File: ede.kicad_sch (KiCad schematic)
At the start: 111 parts, among them J1 Conn_01x01, J10 Conn_01x01, J11 Conn_01x01, J12 Conn_01x01, J2 Conn_01x01, J3 Conn_01x01, J4 Conn_01x01, J5 Conn_01x06, J6 Conn_01x01, J7 Conn_01x04, J8 Conn_01x04, J9 Conn_01x01, Q1 MDP10N027, Q2 MDP10N027, Q3 MDP10N027, Q4 MDP10N027, Q5 MDP10N027, Q6 MDP10N027, U1 YAAJ_BluePill, U2 NCS20034DR2G, U3 STH0548S12, U4 MP1584EN_4pin, U5 U3216, U6 U3216, U7 U3216

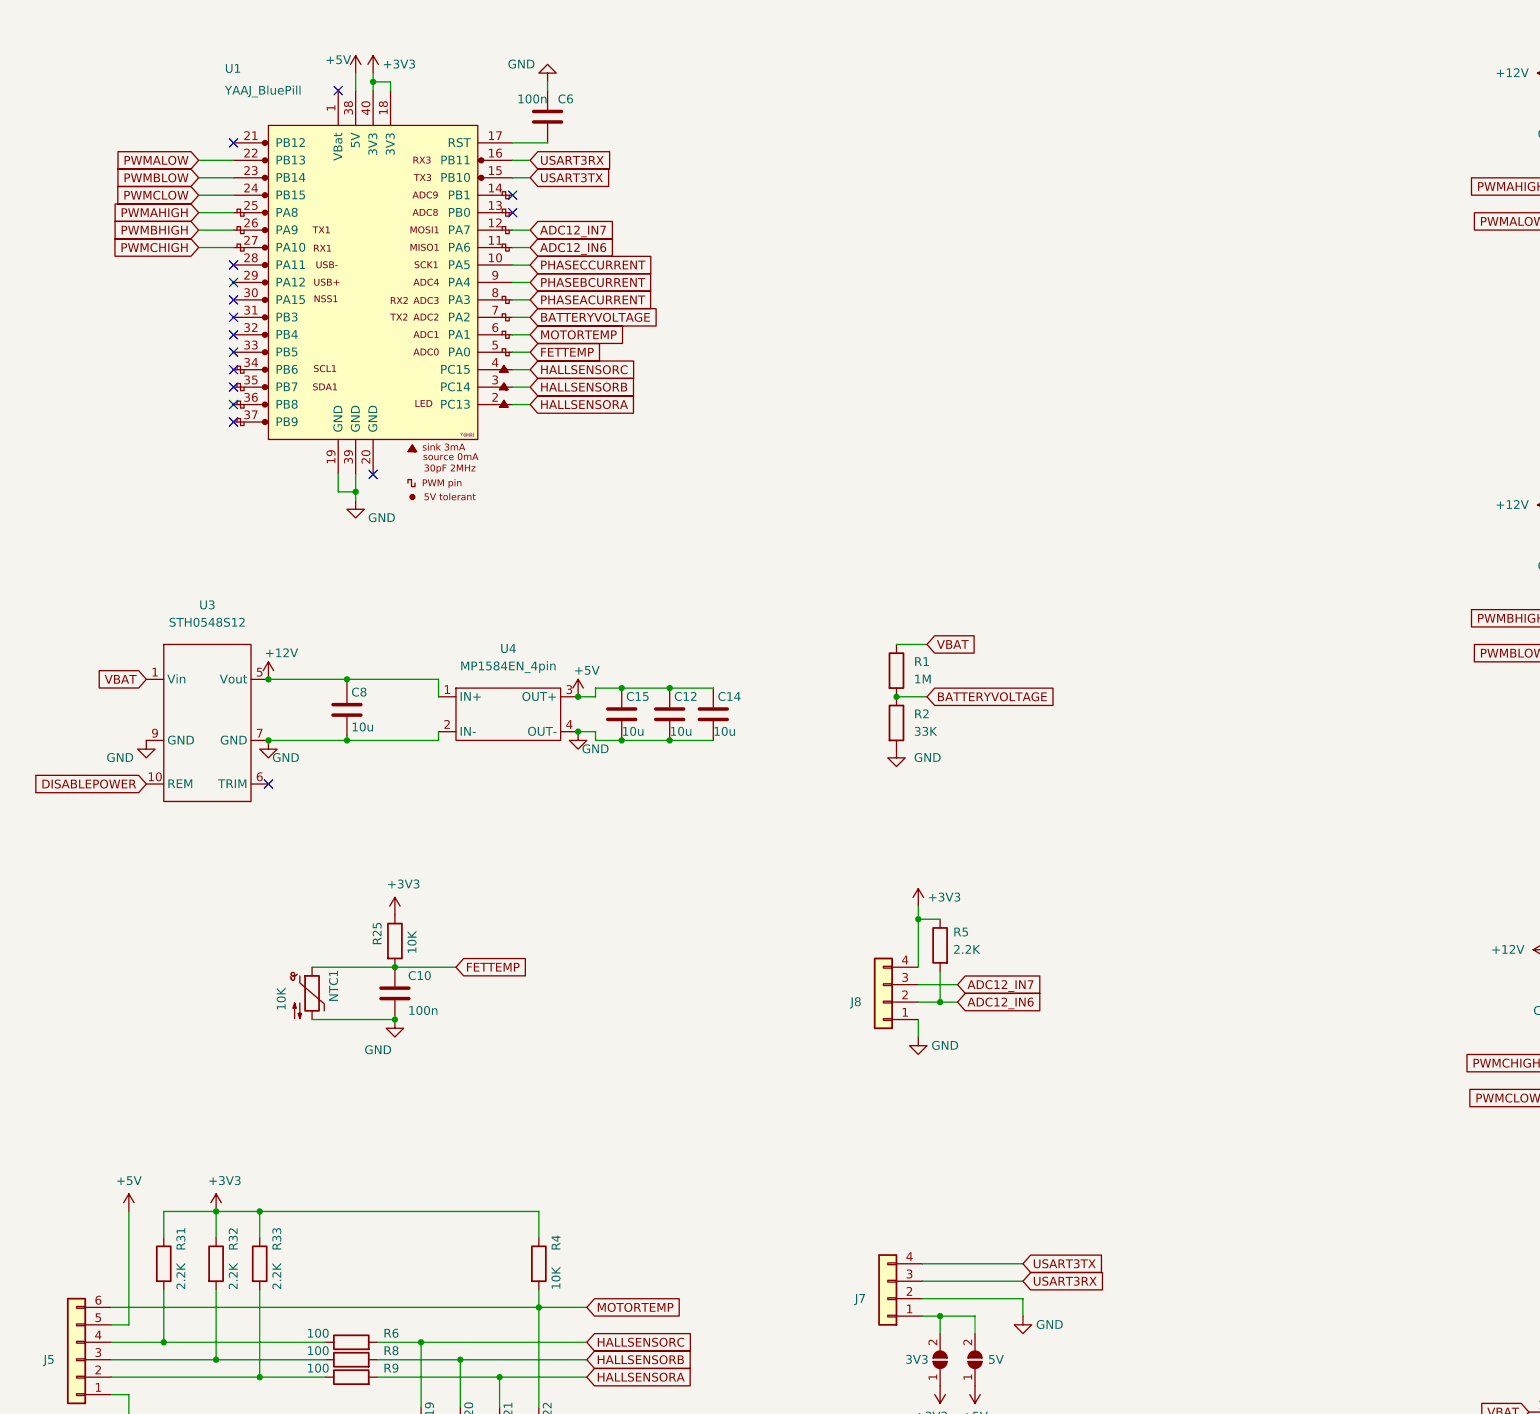
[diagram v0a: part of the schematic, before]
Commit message: sch: blackpill instead of bluepill
Firmware for this project only supports blackpill ATM. Reflect it in
schematic, note pcb layout used is same as in v0.5.x .

Signed-off-by: Afzal <afzal@intible.in>
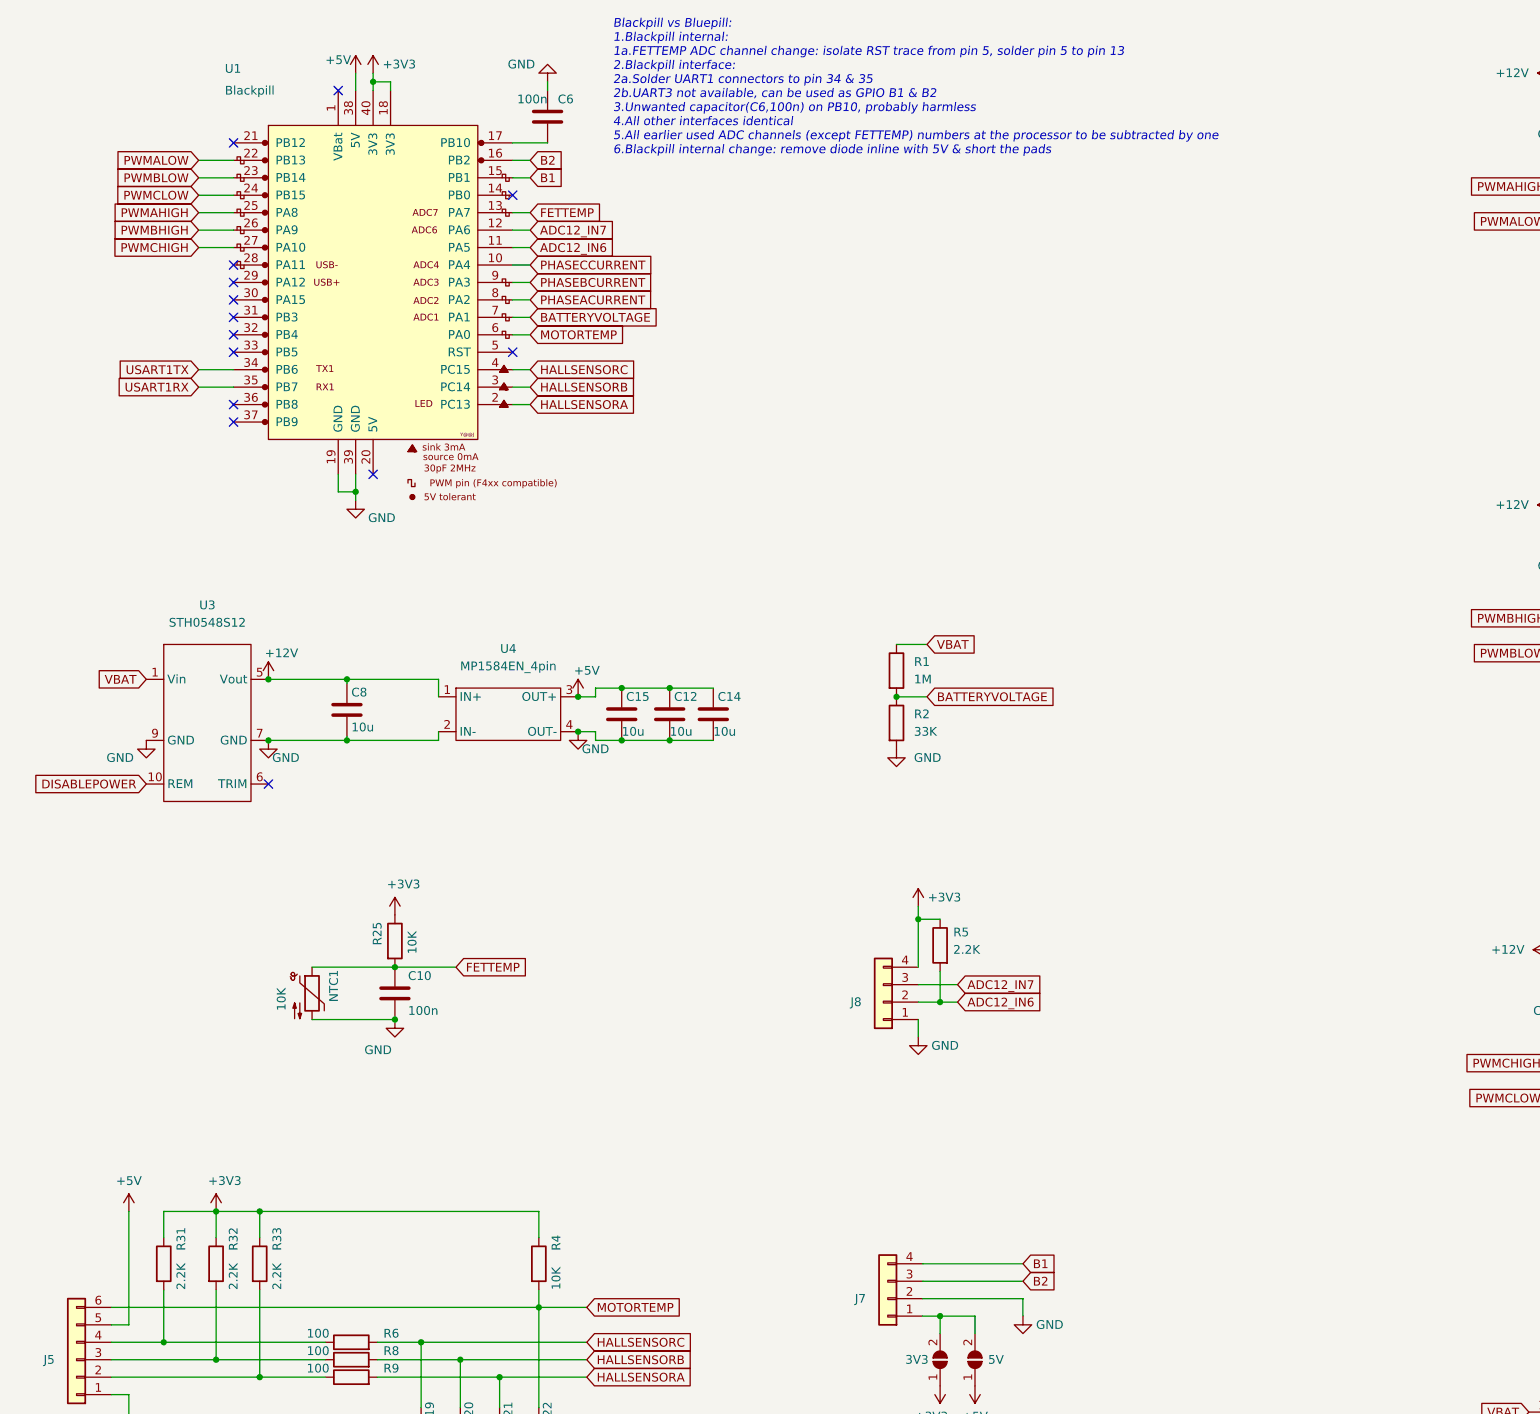
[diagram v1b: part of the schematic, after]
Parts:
- U1: value YAAJ_BluePill -> Blackpill; footprint Intible:YAAJ_Bluepill -> (none); symbol Bluepill_Module:YAAJ_BluePill -> Bluepill_Module:Blackpill; now in the parts list
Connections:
- net FETTEMP: now also U1.13 (PA7); no longer U1.5 (PA0)
- net USART1TX: now reaches U1.34 (PB6)
- net USART1RX: now reaches U1.35 (PB7)
- net USART3RX renamed B2
- net USART3TX renamed B1
- no-connect marks 16 -> 14
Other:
- note added: "Blackpill vs Bluepill: 1.Blackpill internal: 1a.FETTEMP ADC channel change: isolate RST trace from pin 5, solder pin 5 to pin 13 2.Blackpill interface: 2a.Solder UART1 connectors to pin 34 & 35 2b.UART3 not available, can be used as GPIO B1 & B2 3.Unwanted capacitor(C6,100n) on PB10, probably harmless 4.All other interfaces identical 5.All earlier used ADC channels (except FETTEMP) numbers at the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"
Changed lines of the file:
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@@
   (no_connect (at 46.99 50.8))
   (no_connect (at 46.99 48.26))
-  (no_connect (at 87.63 40.64))
   (no_connect (at 62.23 22.86))
   (no_connect (at 87.63 38.1))
@@
   (no_connect (at 46.99 53.34))
   (no_connect (at 46.99 58.42))
-  (no_connect (at 46.99 63.5))
   (no_connect (at 46.99 68.58))
   (no_connect (at 46.99 60.96))
-  (no_connect (at 46.99 66.04))
   (no_connect (at 46.99 30.48))
   (no_connect (at 46.99 71.12))
+  (no_connect (at 87.63 60.96))
   (wire (pts (xy 50.8 186.055) (xy 50.8 189.865))
     (stroke (width 0) (type default) (color 0 0 0 0))
@@
     (stroke (width 0) (type default) (color 0 0 0 0))
   )
+  (wire (pts (xy 41.91 63.5) (xy 46.99 63.5))
+    (stroke (width 0) (type default) (color 0 0 0 0))
+  )
   (wire (pts (xy 110.49 117.475) (xy 103.505 117.475))
     (stroke (width 0) (type default) (color 0 0 0 0))
@@
     (stroke (width 0) (type default) (color 0 0 0 0))
   )
+  (wire (pts (xy 41.91 66.04) (xy 46.99 66.04))
+    (stroke (width 0) (type default) (color 0 0 0 0))
+  )
   (wire (pts (xy 313.055 38.1) (xy 313.055 40.64))
     (stroke (width 0) (type default) (color 0 0 0 0))
@@
     (stroke (width 0) (type default) (color 0 0 0 0))
   )
+  (wire (pts (xy 87.63 35.56) (xy 90.17 35.56))
+    (stroke (width 0) (type default) (color 0 0 0 0))
+  )
   (wire (pts (xy 286.385 90.805) (xy 290.195 90.805))
     (stroke (width 0) (type default) (color 0 0 0 0))
@@
     (stroke (width 0) (type default) (color 0 0 0 0))
   )
-  (wire (pts (xy 87.63 35.56) (xy 90.17 35.56))
-    (stroke (width 0) (type default) (color 0 0 0 0))
-  )
   (wire (pts (xy 41.91 35.56) (xy 46.99 35.56))
     (stroke (width 0) (type default) (color 0 0 0 0))
@@
     (stroke (width 0) (type default) (color 0 0 0 0))
   )
+  (wire (pts (xy 87.63 40.64) (xy 90.17 40.64))
+    (stroke (width 0) (type default) (color 0 0 0 0))
+  )
   (wire (pts (xy 302.895 118.745) (xy 313.055 118.745))
     (stroke (width 0) (type default) (color 0 0 0 0))
@@
     (stroke (width 0) (type default) (color 0 0 0 0))
   )
+  (wire (pts (xy 87.63 33.02) (xy 90.17 33.02))
+    (stroke (width 0) (type default) (color 0 0 0 0))
+  )
   (wire (pts (xy 238.76 164.465) (xy 250.19 164.465))
     (stroke (width 0) (type default) (color 0 0 0 0))
@@
     (stroke (width 0) (type default) (color 0 0 0 0))
   )
-  (wire (pts (xy 87.63 60.96) (xy 90.17 60.96))
-    (stroke (width 0) (type default) (color 0 0 0 0))
-  )
   (wire (pts (xy 250.19 169.545) (xy 250.19 168.275))
     (stroke (width 0) (type default) (color 0 0 0 0))
@@
     (stroke (width 0) (type default) (color 0 0 0 0))
   )
-  (wire (pts (xy 87.63 33.02) (xy 90.17 33.02))
-    (stroke (width 0) (type default) (color 0 0 0 0))
-  )
   (wire (pts (xy 272.415 30.48) (xy 272.415 20.32))
     (stroke (width 0) (type default) (color 0 0 0 0))
@@
     (stroke (width 0) (type default) (color 0 0 0 0))
   )
+  (text "Blackpill vs Bluepill:\n1.Blackpill internal:\n1a.FETTEMP ADC channel change: isolate RST trace from pin 5, solder pin 5 to pin 13\n2.Blackpill interface:\n2a.Solder UART1 connectors to pin 34 & 35\n2b.UART3 not available, can be used as GPIO B1 & B2\n3.Unwanted capacitor(C6,100n) on PB10, probably harmless \n4.All other interfaces identical\n5.All earlier used ADC channels (except FETTEMP) numbers at the processor to be subtracted by one\n6.Blackpill internal change: remove diode inline with 5V & short the pads"
+    (at 102.235 32.385 0)
+    (effects (font (size 1.27 1.27) italic) (justify left bottom))
+  )
   (label "GL_B" (at 300.355 108.585 0)
     (effects (font (size 1.27 1.27)) (justify left bottom))
@@
     )
   )
+  (global_label "USART1TX" (shape input) (at 41.91 63.5 180) (fields_autoplaced)
+    (effects (font (size 1.27 1.27)) (justify right))
+    (property "Intersheet References" "${INTERSHEET_REFS}" (id 0) (at 30.244 63.4206 0)
+      (effects (font (size 1.27 1.27)) (justify right) hide)
+    )
+  )
   (global_label "DISABLEPOWER" (shape input) (at 34.29 123.825 180) (fields_autoplaced)
     (effects (font (size 1.27 1.27)) (justify right))
@@
     )
   )
-  (global_label "USART3RX" (shape input) (at 161.925 196.215 0) (fields_autoplaced)
+  (global_label "B2" (shape input) (at 161.925 196.215 0) (fields_autoplaced)
     (effects (font (size 1.27 1.27)) (justify left))
-    (property "Intersheet References" "${INTERSHEET_REFS}" (id 0) (at 173.8933 196.1356 0)
+    (property "Intersheet References" "${INTERSHEET_REFS}" (id 0) (at 166.8176 196.1356 0)
       (effects (font (size 1.27 1.27)) (justify left) hide)
     )
@@
     )
   )
+  (global_label "B2" (shape input) (at 90.17 33.02 0) (fields_autoplaced)
+    (effects (font (size 1.27 1.27)) (justify left))
+    (property "Intersheet References" "${INTERSHEET_REFS}" (id 0) (at 95.0626 32.9406 0)
+      (effects (font (size 1.27 1.27)) (justify left) hide)
+    )
+  )
   (global_label "VBAT" (shape input) (at 273.05 269.24 270) (fields_autoplaced)
     (effects (font (size 1.27 1.27)) (justify right))
@@
     )
   )
-  (global_label "USART3TX" (shape input) (at 161.925 193.675 0) (fields_autoplaced)
+  (global_label "B1" (shape input) (at 161.925 193.675 0) (fields_autoplaced)
     (effects (font (size 1.27 1.27)) (justify left))
-    (property "Intersheet References" "${INTERSHEET_REFS}" (id 0) (at 173.591 193.5956 0)
+    (property "Intersheet References" "${INTERSHEET_REFS}" (id 0) (at 166.8176 193.5956 0)
       (effects (font (size 1.27 1.27)) (justify left) hide)
     )
@@
     )
   )
+  (global_label "USART1RX" (shape input) (at 41.91 66.04 180) (fields_autoplaced)
+    (effects (font (size 1.27 1.27)) (justify right))
+    (property "Intersheet References" "${INTERSHEET_REFS}" (id 0) (at 29.9417 65.9606 0)
+      (effects (font (size 1.27 1.27)) (justify right) hide)
+    )
+  )
   (global_label "VBIAS" (shape input) (at 370.84 108.585 0) (fields_autoplaced)
     (effects (font (size 1.27 1.27)) (justify left))
@@
     )
   )
-  (global_label "USART3TX" (shape input) (at 90.17 35.56 0) (fields_autoplaced)
+  (global_label "B1" (shape input) (at 90.17 35.56 0) (fields_autoplaced)
     (effects (font (size 1.27 1.27)) (justify left))
-    (property "Intersheet References" "${INTERSHEET_REFS}" (id 0) (at 101.836 35.4806 0)
+    (property "Intersheet References" "${INTERSHEET_REFS}" (id 0) (at 95.0626 35.4806 0)
       (effects (font (size 1.27 1.27)) (justify left) hide)
     )
@@
     )
   )
-  (global_label "FETTEMP" (shape input) (at 90.17 60.96 0) (fields_autoplaced)
+  (global_label "FETTEMP" (shape input) (at 90.17 40.64 0) (fields_autoplaced)
     (effects (font (size 1.27 1.27)) (justify left))
-    (property "Intersheet References" "${INTERSHEET_REFS}" (id 0) (at 100.6264 60.8806 0)
+    (property "Intersheet References" "${INTERSHEET_REFS}" (id 0) (at 100.6264 40.5606 0)
       (effects (font (size 1.27 1.27)) (justify left) hide)
     )
@@
     )
   )
-  (global_label "USART3RX" (shape input) (at 90.17 33.02 0) (fields_autoplaced)
-    (effects (font (size 1.27 1.27)) (justify left))
-    (property "Intersheet References" "${INTERSHEET_REFS}" (id 0) (at 102.1383 32.9406 0)
-      (effects (font (size 1.27 1.27)) (justify left) hide)
-    )
-  )
   (symbol (lib_id "Device:C") (at 110.49 113.665 0) (unit 1)
     (in_bom yes) (on_board yes)
@@
     (pin "2")
   )
-  (symbol (lib_id "Bluepill_Module:YAAJ_BluePill") (at 67.31 50.8 0) (unit 1)
-    (in_bom no) (on_board yes)
+  (symbol (lib_id "Bluepill_Module:Blackpill") (at 67.31 50.8 0) (unit 1)
+    (in_bom yes) (on_board yes)
     (property "Reference" "U1" (id 0) (at 45.72 19.685 0)
       (effects (font (size 1.27 1.27)) (justify left))
     )
-    (property "Value" "YAAJ_BluePill" (id 1) (at 45.72 22.86 0)
+    (property "Value" "Blackpill" (id 1) (at 45.72 22.86 0)
       (effects (font (size 1.27 1.27)) (justify left))
     )
-    (property "Footprint" "Intible:YAAJ_Bluepill" (id 2) (at 65.405 26.67 90)
+    (property "Footprint" "" (id 2) (at 65.405 26.67 90)
       (effects (font (size 1.27 1.27)) hide)
     )
@@
     )
     (path "/a9708a6e-3a56-44b9-b1fc-15d528ecac3e"
-      (reference "U1") (unit 1) (value "YAAJ_BluePill") (footprint "Intible:YAAJ_Bluepill")
+      (reference "U1") (unit 1) (value "Blackpill") (footprint "")
     )
     (path "/2adc3a9f-6d7f-41d9-b1d6-fc8b7b806926"

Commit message: sch: assign bluepill fp for blackpill temporarily
Signed-off-by: Afzal <afzal@intible.in>
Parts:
- U1: footprint (none) -> Intible:YAAJ_Bluepill
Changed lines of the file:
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@@
       (effects (font (size 1.27 1.27)) (justify left))
     )
-    (property "Footprint" "" (id 2) (at 65.405 26.67 90)
+    (property "Footprint" "Intible:YAAJ_Bluepill" (id 2) (at 65.405 26.67 90)
       (effects (font (size 1.27 1.27)) hide)
     )
@@
     )
     (path "/a9708a6e-3a56-44b9-b1fc-15d528ecac3e"
-      (reference "U1") (unit 1) (value "Blackpill") (footprint "")
+      (reference "U1") (unit 1) (value "Blackpill") (footprint "Intible:YAAJ_Bluepill")
     )
     (path "/2adc3a9f-6d7f-41d9-b1d6-fc8b7b806926"
